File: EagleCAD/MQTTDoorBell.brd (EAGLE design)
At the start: 95.2 x 23.5 mm, 17 parts, among them Q1 MMBT2222

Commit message: updating design and starting to structure board
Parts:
- removed C4: (no value), adafruit:E5-13
- moved X1 81.3 mm to (10.2, 50.8), turned to 0 degrees
- moved JP1 42.6 mm to (16.5, 24.1), turned to 0 degrees
- moved C3 23.6 mm to (29.2, 27.9), turned to 90 degrees
- moved C5 21.6 mm to (9.91, 23.5)
- moved C2 17.6 mm to (10.2, 35.6)
- moved BR1 11.4 mm to (5.46, 29.0), turned to 180 degrees
- moved U$1 8.70 mm to (20.3, 9.14)
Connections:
- removed net BELL_OUT1: J1.5
- net 16V_AC1: now also J1.5
- net 16V_AC2: now also U$1.1
- net 3.3V: no longer C4.+
- net BELL_OUT2: now also U$1.4
- net BUTTON1: now also X1.4
- net GND: no longer C4.-
- net RELAYSIGNAL: now also X1.12
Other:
- board size 95.2 x 23.5 mm -> 71.1 x 64.2 mm

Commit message: initial commit of eagle files, version 1 of board'
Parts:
- removed C3: (no value), adafruit:E5-13
- removed J1: (no value), SparkFun-Connectors:SCREWTERMINAL-3.5MM-6
- removed JP1: (no value), adafruit:1X03-CLEANBIG
- added C4: 10uf, SparkFun-Capacitors:0805
- added C7: (no value), adafruit:E5-10,5
- added J2: (no value), SparkFun-Connectors:SCREWTERMINAL-3.5MM-2
- added J3: (no value), SparkFun-Connectors:SCREWTERMINAL-3.5MM-4
- added PROG: (no value), SparkFun-Connectors:1X05
- added R6, R7: 2K, microbuilder:0805-NO
- added SW2: SPST_TACT-EVQQ2, adafruit:EVQ-Q2
- added U1: TSR_1-2433, Traco_TSR:TSR-1
- R1, R2, R3: value (none) -> 10k
- moved X1 64.4 mm to (65.0, 17.0), turned to 270 degrees
- moved D1 14.8 mm to (33.0, 9.00), turned to 270 degrees
- moved C2 13.9 mm to (13.0, 22.0)
- moved R3 12.0 mm to (54.0, 6.00)
- moved C1 10.9 mm to (52.0, 14.0), turned to 270 degrees
- moved R5 9.36 mm to (41.0, 11.0), turned to 270 degrees
- moved Q1 9.05 mm to (37.0, 9.00), turned to 90 degrees
- moved R1 9.00 mm to (59.0, 6.00), turned to 180 degrees
- moved BR1 7.97 mm to (5.00, 21.0)
- moved R4 4.51 mm to (44.0, 11.0), turned to 270 degrees
- moved R2 3.89 mm to (64.0, 6.00), turned to 180 degrees
- moved C5 1.50 mm to (10.0, 22.0), turned to 90 degrees
- moved U$1 1.00 mm to (19.3, 9.14)
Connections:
- removed net BUTTON2: J1.4
- new net GPIO0: PROG.2, X1.12
- new net RELAYDETECT: R6.2, X1.13
- new net RESET: R7.1, SW2.B, SW2.B', X1.1
- net 16V_AC1: now also J3.1; no longer J1.1, J1.5
- net 16V_AC2: now also J3.2, J3.3; no longer J1.2
- net 16V_DC: now also C7.+, U1.1; no longer C3.+, JP1.1
- net 3.3V: now also C4.1, J2.1, PROG.1, R7.2, U1.3; no longer JP1.3
- net BELL_OUT2: now also J3.4; no longer J1.6
- net BUTTON1: no longer J1.3
- net GND: now also C4.2, C7.-, PROG.5, SW2.A, SW2.A', U1.2; no longer C3.-, JP1.2
- net GPIO15: now also X1.10
- net GPIO2: now also X1.11
- net RELAYSIGNAL: now also J2.2, R6.1; no longer X1.12
- net RX: now also PROG.3
- net TX: now also PROG.4
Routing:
- net GND: track 0.00 -> 109.4 mm, vias 0 -> 2
- net 3.3V: track 0.00 -> 100.3 mm, vias 0 -> 1
- net RESET: track 0.00 -> 37.6 mm
- net 16V_AC2: track 0.00 -> 34.8 mm
- net 16V_DC: track 0.00 -> 29.3 mm
- net CH_PD: track 0.00 -> 19.0 mm
- net N$4: track 0.00 -> 14.0 mm
- net RELAYDETECT: track 0.00 -> 13.8 mm
- net RELAYSIGNAL: track 0.00 -> 11.9 mm
- net GPIO0: track 0.00 -> 10.3 mm
- net BELL_OUT2: track 0.00 -> 9.73 mm
- net TX: track 0.00 -> 8.80 mm
- net RX: track 0.00 -> 8.56 mm
- net N$22: track 0.00 -> 6.87 mm
- net GPIO15: track 0.00 -> 4.58 mm
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- added copper zone on layer 1, net ACISO1
- added copper zone on layer 16, net ACISO1
- added copper zone on layer 1, net GND
- added copper zone on layer 16, net GND
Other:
- board size 71.1 x 64.2 mm -> 78 x 27 mm

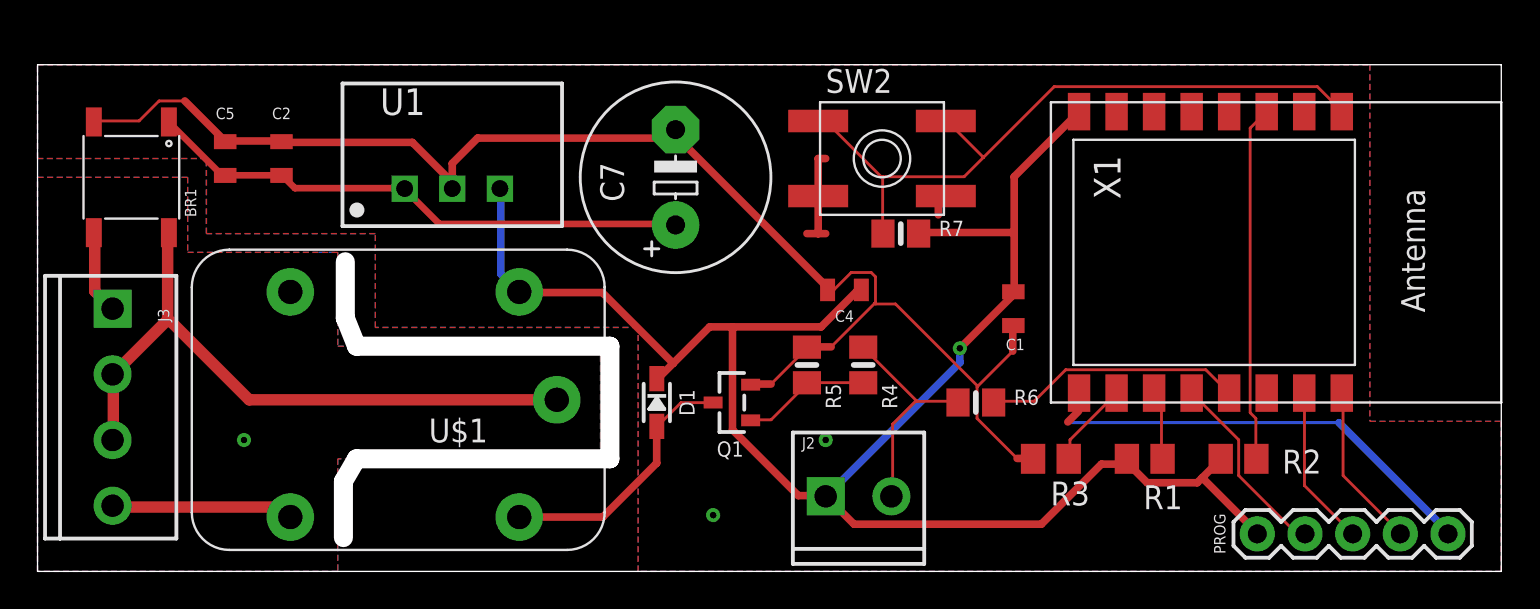
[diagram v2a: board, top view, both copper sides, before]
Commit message: fix polygon issue and add labels'
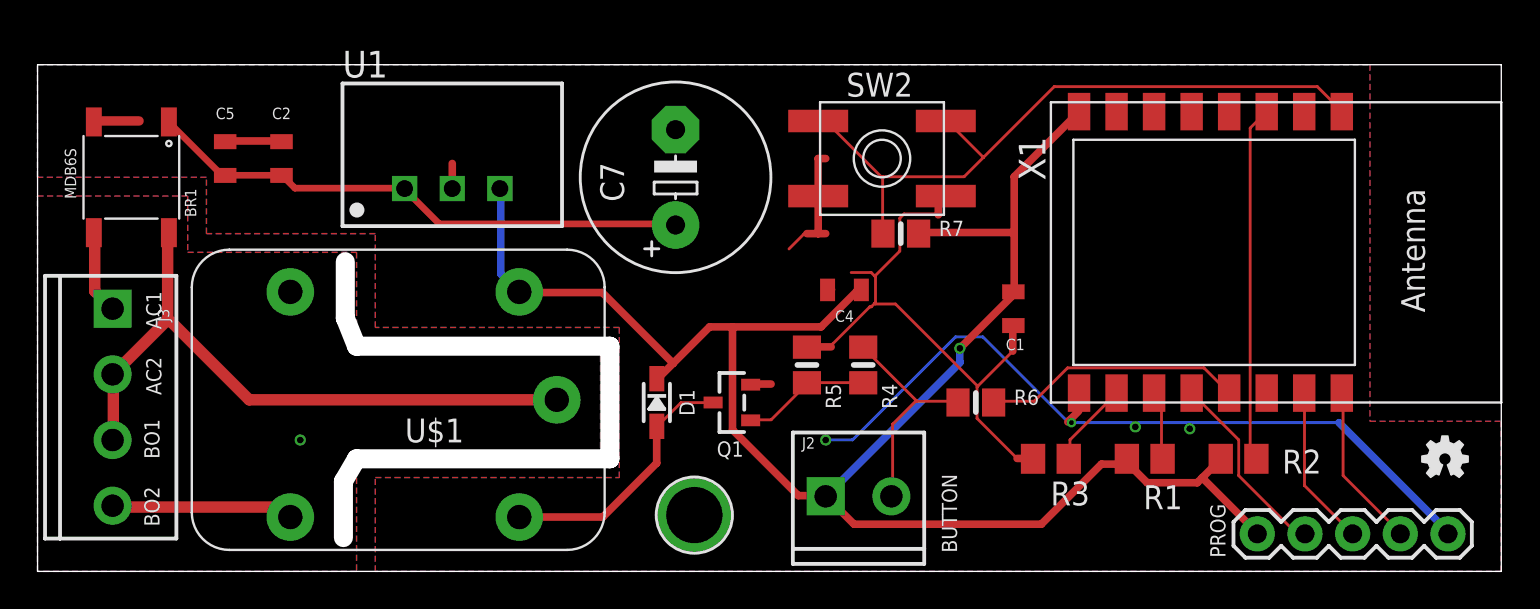
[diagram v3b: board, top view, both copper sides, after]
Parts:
- added LOGO1: OSHW-LOGOMINI, SparkFun-Aesthetics:OSHW-LOGO-MINI
- added LOGO2: ROHS_LOGO, SparkFun-Aesthetics:ROHS_LOGO_0.18_IN
- added U$4: MICROBUILDER_MOUNTINGHOLE3.0THIN, microbuilder:MICROBUILDER_MOUNTINGHOLE_3.0_PLATEDTHIN
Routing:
- net GND: track 109.4 -> 90.2 mm, vias 2 -> 4
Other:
- board text added: "1/22/2019"
- board text added: "AC1"
- board text added: "AC2"
- board text added: "BO1"
- board text added: "BO2"
- board text added: "BUTTON"
- board text added: "MQTT DoorBell"
- board text added: "v1.0"
- board text added: "www.jaycollett.com"

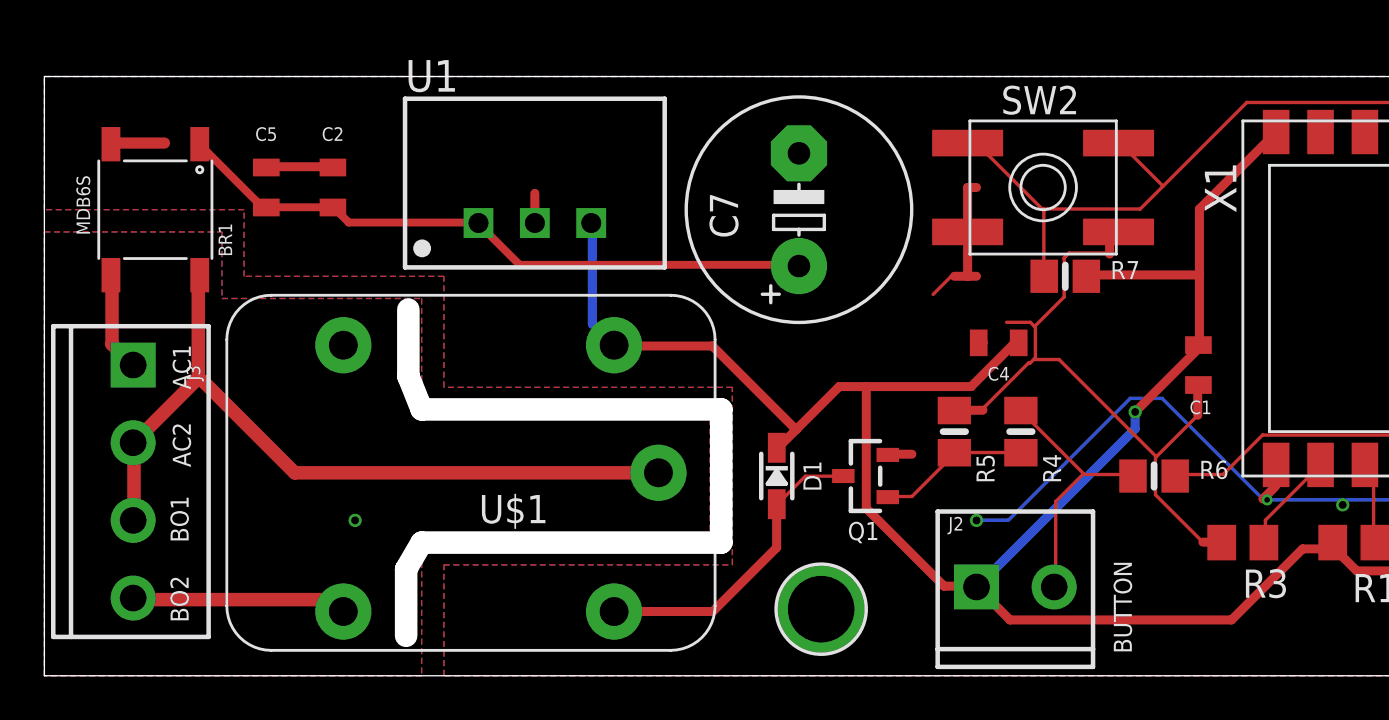
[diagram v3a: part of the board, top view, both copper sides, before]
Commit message: add new PCB board and schematic, add first draf of firmware
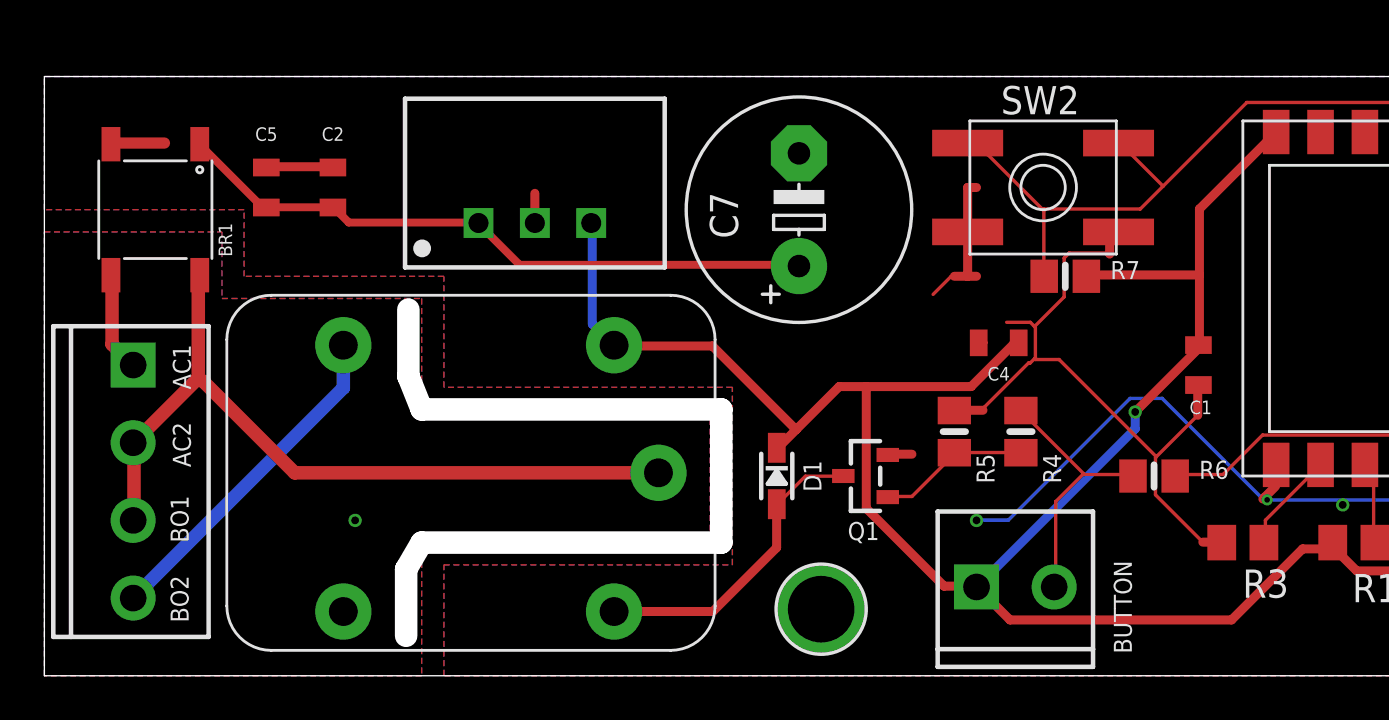
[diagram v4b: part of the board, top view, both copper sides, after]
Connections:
- net BELL_OUT2: now also U$1.3; no longer U$1.4
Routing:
- net BELL_OUT2: track 9.73 -> 15.4 mm
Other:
- board text added: "2/3/2019"
- board text added: "v1.4"
- board text removed: "1/22/2019"
- board text removed: "v1.0"

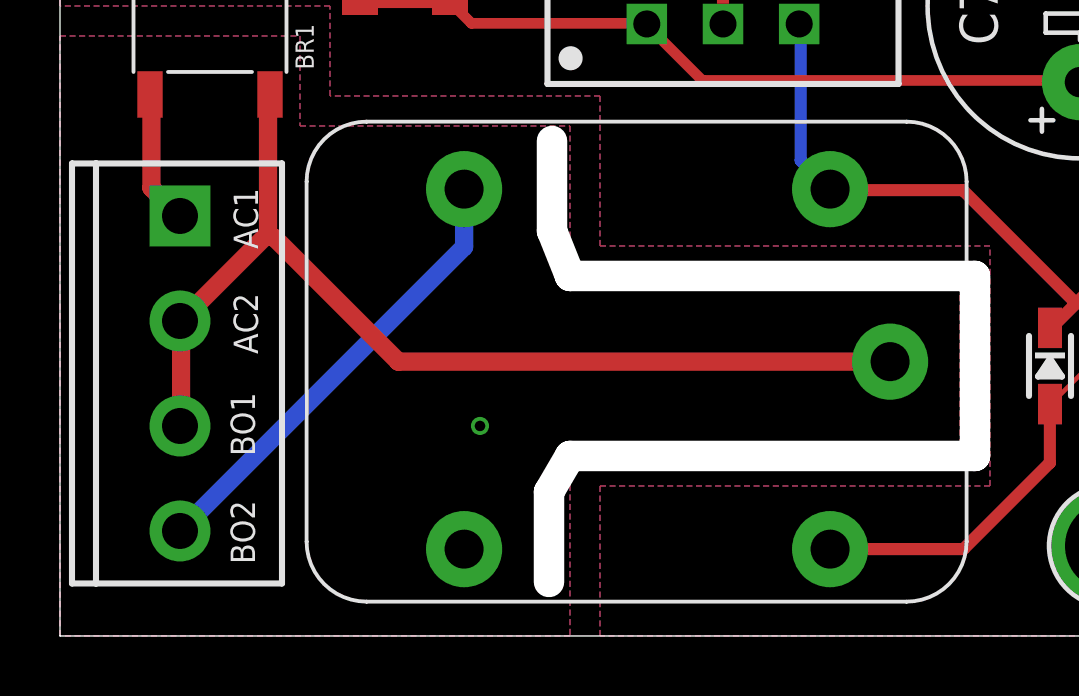
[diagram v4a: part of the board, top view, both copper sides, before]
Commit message: fixing critical error with AC power lines to doorbell ringer
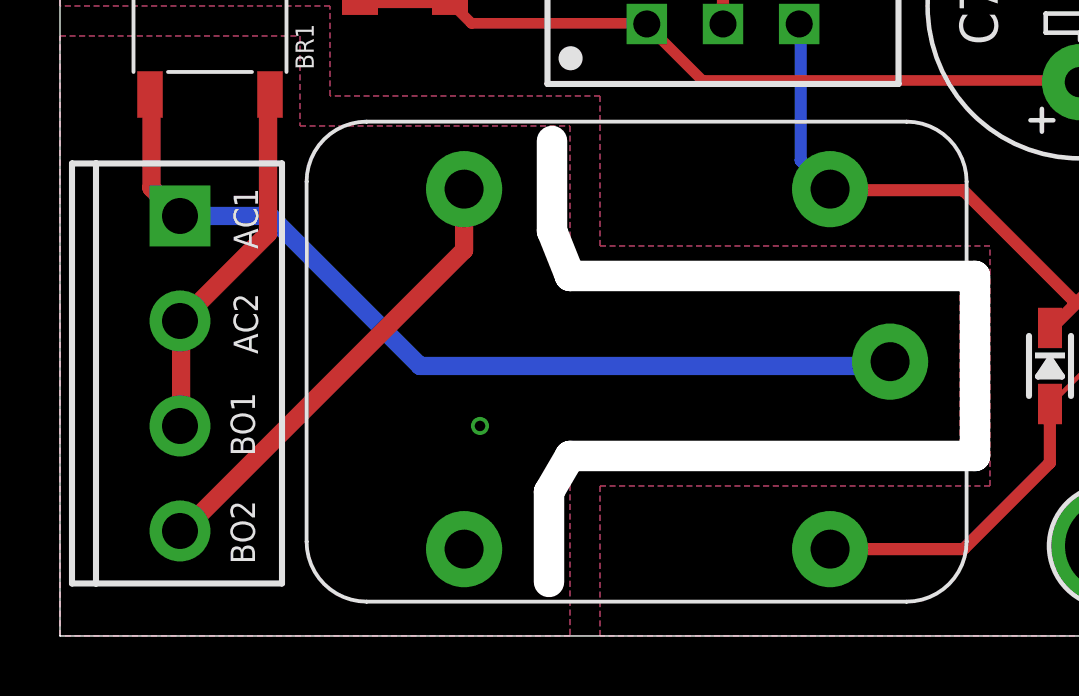
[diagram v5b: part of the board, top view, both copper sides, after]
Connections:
- net 16V_AC1: now also U$1.1
- net 16V_AC2: no longer U$1.1
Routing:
- net 16V_AC1: track 4.47 -> 30.3 mm
- net 16V_AC2: track 34.8 -> 12.3 mm
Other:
- board text added: "2/17/2019"
- board text added: "v1.5"
- board text removed: "2/3/2019"
- board text removed: "v1.4"
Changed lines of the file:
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@@
 <text x="77" y="25" size="1.27" layer="22" rot="MR0">www.jaycollett.com</text>
 <text x="77.2" y="22.9" size="1.27" layer="22" rot="MR0">MQTT DoorBell</text>
-<text x="77" y="21" size="1.27" layer="22" rot="MR0">v1.4</text>
-<text x="77" y="18.6" size="1.27" layer="22" rot="MR0">2/3/2019</text>
+<text x="77" y="21" size="1.27" layer="22" rot="MR0">v1.5</text>
+<text x="77" y="18.6" size="1.27" layer="22" rot="MR0">2/17/2019</text>
 </plain>
 <attributes>
@@
 <signal name="16V_AC2" class="2">
 <contactref element="BR1" pad="AC1"/>
-<contactref element="U$1" pad="1"/>
 <contactref element="J3" pad="2"/>
 <contactref element="J3" pad="3"/>
@@
 <wire x1="4.0386" y1="7.0104" x2="4" y2="7" width="0.6096" layer="1"/>
 <wire x1="4.0386" y1="10.2108" x2="4" y2="10.5" width="0.6096" layer="1"/>
-<wire x1="11.2776" y1="9.144" x2="27.67" y2="9.144" width="0.6096" layer="1"/>
-<wire x1="7.1628" y1="13.2588" x2="11.2776" y2="9.144" width="0.6096" layer="1"/>
-<wire x1="7.1628" y1="13.2588" x2="6.9342" y2="13.4112" width="0.6096" layer="1"/>
 </signal>
 <signal name="BUTTON1">
@@
 <wire x1="4.0386" y1="3.429" x2="4" y2="3.5" width="0.6096" layer="1"/>
 <contactref element="U$1" pad="3"/>
-<wire x1="13.47" y1="14.894" x2="13.47" y2="12.97" width="0.6096" layer="16"/>
-<wire x1="13.47" y1="12.97" x2="4" y2="3.5" width="0.6096" layer="16"/>
+<wire x1="13.47" y1="14.894" x2="13.47" y2="12.8604" width="0.6096" layer="1"/>
+<wire x1="13.47" y1="12.8604" x2="4.0386" y2="3.429" width="0.6096" layer="1"/>
 </signal>
 <signal name="16V_AC1" class="2">
@@
 <wire x1="3.048" y1="17.9832" x2="3" y2="18.05" width="0.6096" layer="1"/>
 <wire x1="3.9624" y1="14.0208" x2="4" y2="14" width="0.6096" layer="1"/>
+<contactref element="U$1" pad="1"/>
+<wire x1="4" y1="14" x2="7" y2="14" width="0.6096" layer="16"/>
+<wire x1="7" y1="14" x2="12" y2="9" width="0.6096" layer="16"/>
+<wire x1="12" y1="9" x2="27.526" y2="9" width="0.6096" layer="16"/>
+<wire x1="27.526" y1="9" x2="27.67" y2="9.144" width="0.6096" layer="16"/>
 </signal>
 <signal name="N$4">
